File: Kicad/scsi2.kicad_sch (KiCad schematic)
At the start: 30 parts, among them J3 TO-LED, J4 TO-MB, J8 TO-A3000-LED, J9 TO-A3000-MB, U10 NCR53c710 SCSI Host Controller, U13 SST39SF010/020/040, Y1 Abracon ACO-50MHz

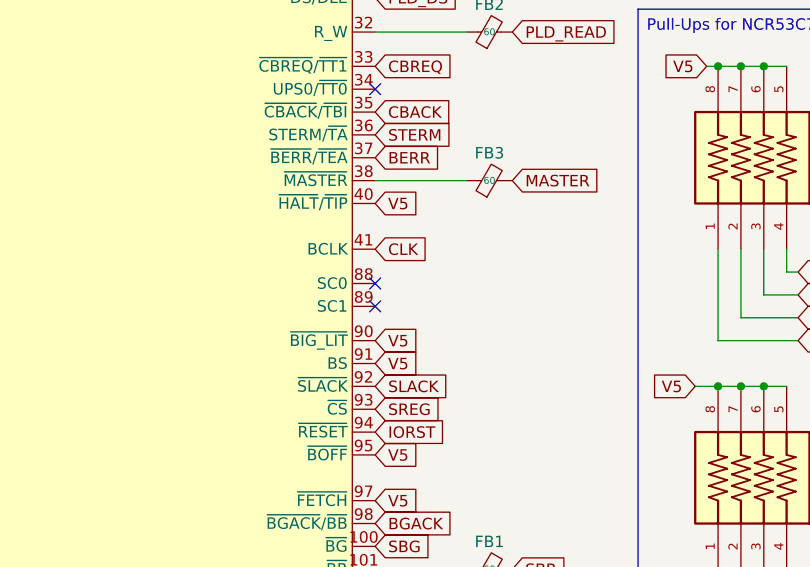
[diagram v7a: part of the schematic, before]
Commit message: Connect SC0 from 53c710 to CPLD
This will let us implement the "False DMA Request Bugfix"
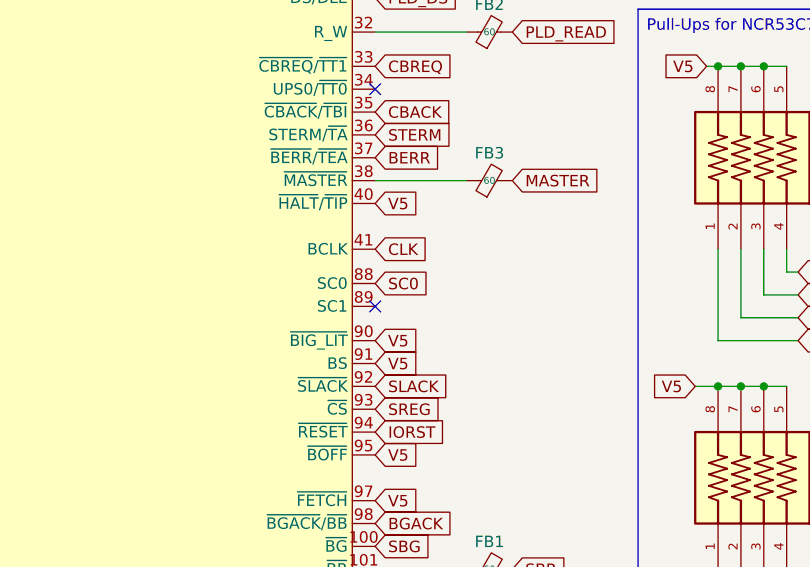
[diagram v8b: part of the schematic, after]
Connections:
- net SC0: now reaches U10.88 (SC0)
- no-connect marks 24 -> 23
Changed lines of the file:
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@@
 	)
 	(no_connect
-		(at 86.36 116.84)
-	)
-	(no_connect
 		(at 151.13 113.03)
 	)
@@
 				(hide yes)
 			)
+		)
+	)
+	(global_label "SC0"
+		(shape input)
+		(at 86.36 116.84 0)
+		(fields_autoplaced yes)
+		(effects
+			(font
+				(size 1.27 1.27)
+			)
+			(justify left)
+		)
+		(property "Intersheetrefs" "${INTERSHEET_REFS}"
+			(at 93.0342 116.84 0)
+			(effects
+				(font
+					(size 1.27 1.27)
+				)
+				(justify left)
+				(hide yes)
+			)
